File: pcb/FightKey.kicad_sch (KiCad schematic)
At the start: 29 parts, among them J1 Conn_01x016_Male

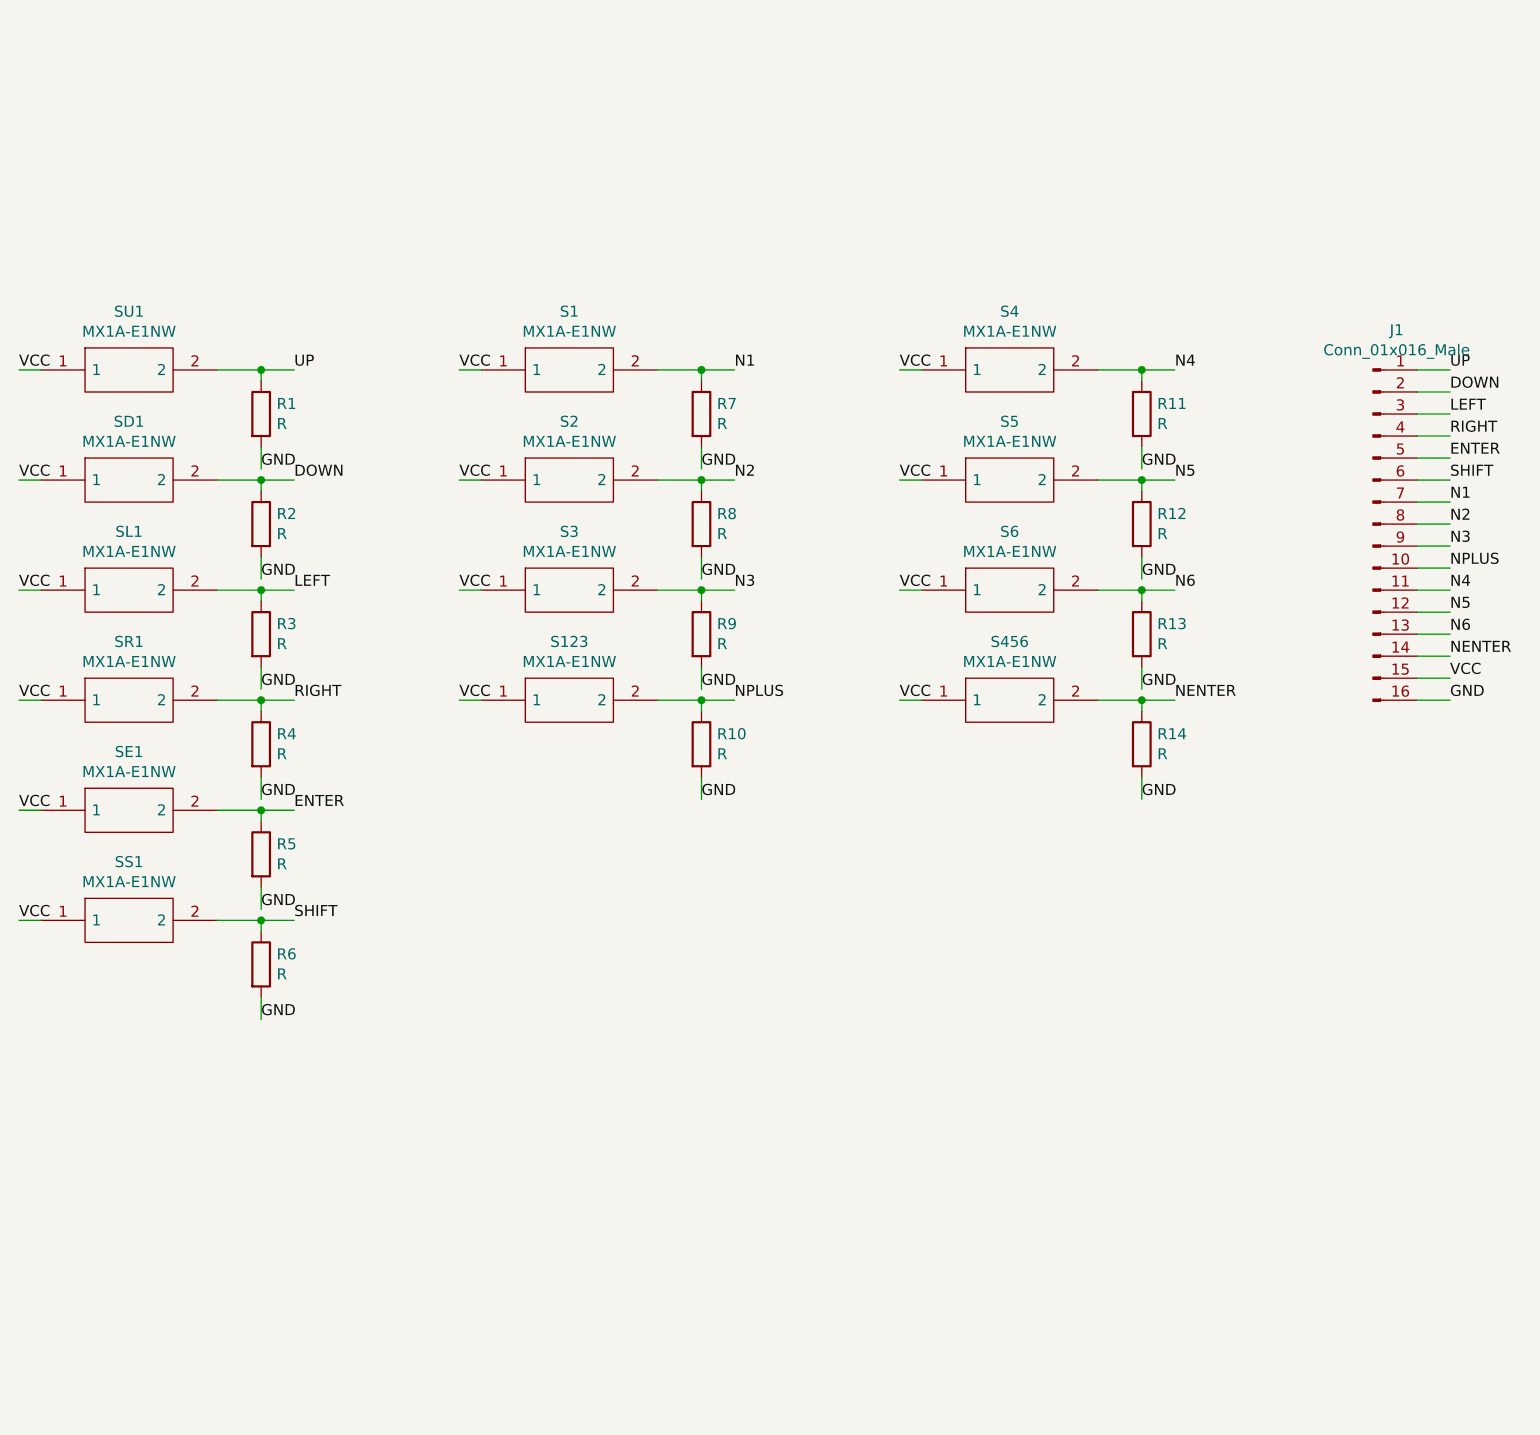
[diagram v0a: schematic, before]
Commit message: Converted to slimmer, openable model with split design (#1)
* Remade PCB to be split and include Pico in design

* Removed stray trace

* Restarted enclosure and modeled out new board left side as a reference

* Fixed missing connection (will have to hotwire physically :(

* Added bottom of enclosure (not done) and modeled right pcb board

* Added top-left of enclosure, left-side rounding, and screw holes

* Added top-right and fixed minor issues. Design complete

* Fixed the keybindings to match expected

* Turned off sys clock increase as it seems to break new pico for some reason

* Readded overclocking, but a decreased amount

* Reworked model polish (screw holes and roundedness stuff

* Fixed key bindings

* Fixed key bindings

* Updated model to fix print issue and increase screw size on incorrect hole

* Fixed some model issues and finished wide version
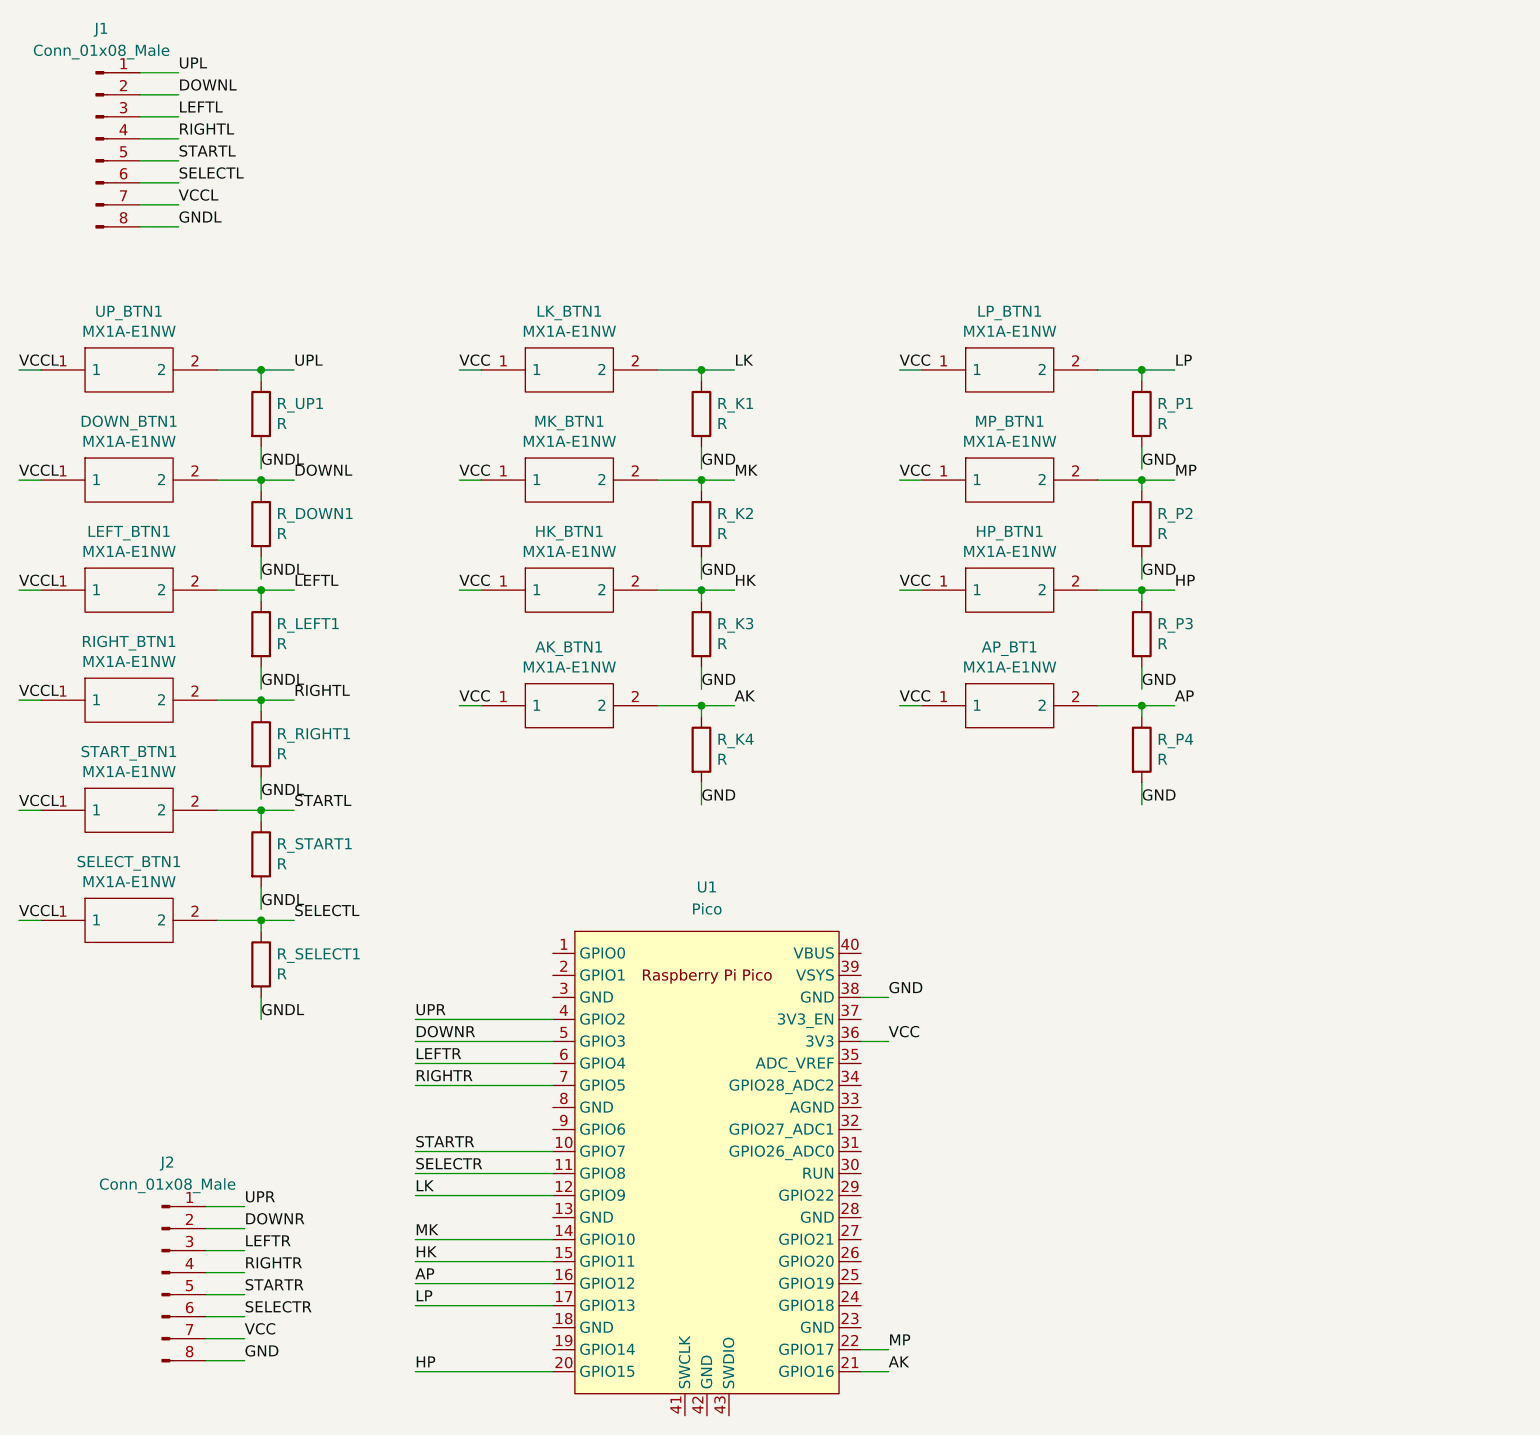
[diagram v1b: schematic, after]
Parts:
- removed J1: Conn_01x016_Male, Connector_PinHeader_2.54mm:PinHeader_1x16_P2.54mm_Vertical, symbol Connector:Conn_01x16_Male
- added J1, J2: Conn_01x08_Male, Connector_PinHeader_2.54mm:PinHeader_1x08_P2.54mm_Vertical, symbol Connector:Conn_01x08_Male
- added U1: Pico, MCU_RaspberryPi_and_Boards:RPi_Pico_SMD_TH, symbol MCU_RaspberryPi_and_Boards:Pico
- renumbered S456 to AK_BTN1, S123 to AP_BT1, SD1 to DOWN_BTN1, S3 to HK_BTN1, S6 to HP_BTN1, SL1 to LEFT_BTN1, S1 to LK_BTN1, S4 to LP_BTN1, S2 to MK_BTN1, S5 to MP_BTN1, SR1 to RIGHT_BTN1, R2 to R_DOWN1, R7 to R_K1, R8 to R_K2, R9 to R_K3, R14 to R_K4, R3 to R_LEFT1, R11 to R_P1, R12 to R_P2, R13 to R_P3, R10 to R_P4, R4 to R_RIGHT1, R6 to R_SELECT1, R5 to R_START1, R1 to R_UP1, SS1 to SELECT_BTN1, SE1 to START_BTN1, SU1 to UP_BTN1
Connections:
- net GND: now also J2.8 (Pin_8), U1.38 (GND); no longer R_DOWN1.2, R_LEFT1.2, R_RIGHT1.2, R_SELECT1.2, R_START1.2, R_UP1.2
- net VCC: now also J2.7 (Pin_7), U1.36 (3V3); no longer DOWN_BTN1.1, LEFT_BTN1.1, RIGHT_BTN1.1, SELECT_BTN1.1, START_BTN1.1, UP_BTN1.1
- net DOWN renamed DOWNL
- net DOWNL: now also J1.2 (Pin_2)
- net ENTER renamed STARTL
- net STARTL: now also J1.5 (Pin_5)
- net LEFT renamed LEFTL
- net LEFTL: now also J1.3 (Pin_3)
- net N1 renamed LK
- net LK: now also U1.12 (GPIO9)
- net N2 renamed MK
- net MK: now also U1.14 (GPIO10)
- net N3 renamed HK
- net HK: now also U1.15 (GPIO11)
- net N4 renamed LP
- net LP: now also U1.17 (GPIO13)
- net N5 renamed MP
- net MP: now also U1.22 (GPIO17)
- net N6 renamed HP
- net HP: now also U1.20 (GPIO15)
- net NENTER renamed AK
- net AK: now also U1.21 (GPIO16)
- net NPLUS renamed AP
- net AP: now also U1.16 (GPIO12)
- net RIGHT renamed RIGHTL
- net RIGHTL: now also J1.4 (Pin_4)
- net SHIFT renamed SELECTL
- net SELECTL: now also J1.6 (Pin_6)
- net UP renamed UPL
- net UPL: now also J1.1 (Pin_1)
- new net DOWNR: J2.2 (Pin_2), U1.5 (GPIO3)
- new net GNDL: J1.8 (Pin_8), R_DOWN1.2, R_LEFT1.2, R_RIGHT1.2, R_SELECT1.2, R_START1.2, R_UP1.2
- new net LEFTR: J2.3 (Pin_3), U1.6 (GPIO4)
- new net RIGHTR: J2.4 (Pin_4), U1.7 (GPIO5)
- new net SELECTR: J2.6 (Pin_6), U1.11 (GPIO8)
- new net STARTR: J2.5 (Pin_5), U1.10 (GPIO7)
- new net UPR: J2.1 (Pin_1), U1.4 (GPIO2)
- new net VCCL: DOWN_BTN1.1, J1.7 (Pin_7), LEFT_BTN1.1, RIGHT_BTN1.1, SELECT_BTN1.1, START_BTN1.1, UP_BTN1.1
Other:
- moved on the sheet: AK_BTN1, AP_BT1, R_K4, R_P4
